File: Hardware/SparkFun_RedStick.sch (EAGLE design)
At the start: 38 parts, among them Q1 DMG2307L, U2 ATMEGA328P_TQFP, U3 CY7C65213, U4 NCP1402, Y1 16MHZ

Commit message: ready for peer review
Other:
- note added: "Boost Regulator"
- note added: "Marshall Taylor"
- note added: "Ports"
- note added: "Power Steering"
- note added: "USB-Serial translation"
- note added: "v01"
- note removed: "3.3v"
- note removed: "5v"
- note removed: "RX (Pin 0)"
- note removed: "TX (Pin 1)"
- note removed: "Voltage Selector"
- moved on the sheet: C10, C11, C3, C4, C5, C6, C7, C8, C9, D1, D2, D3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

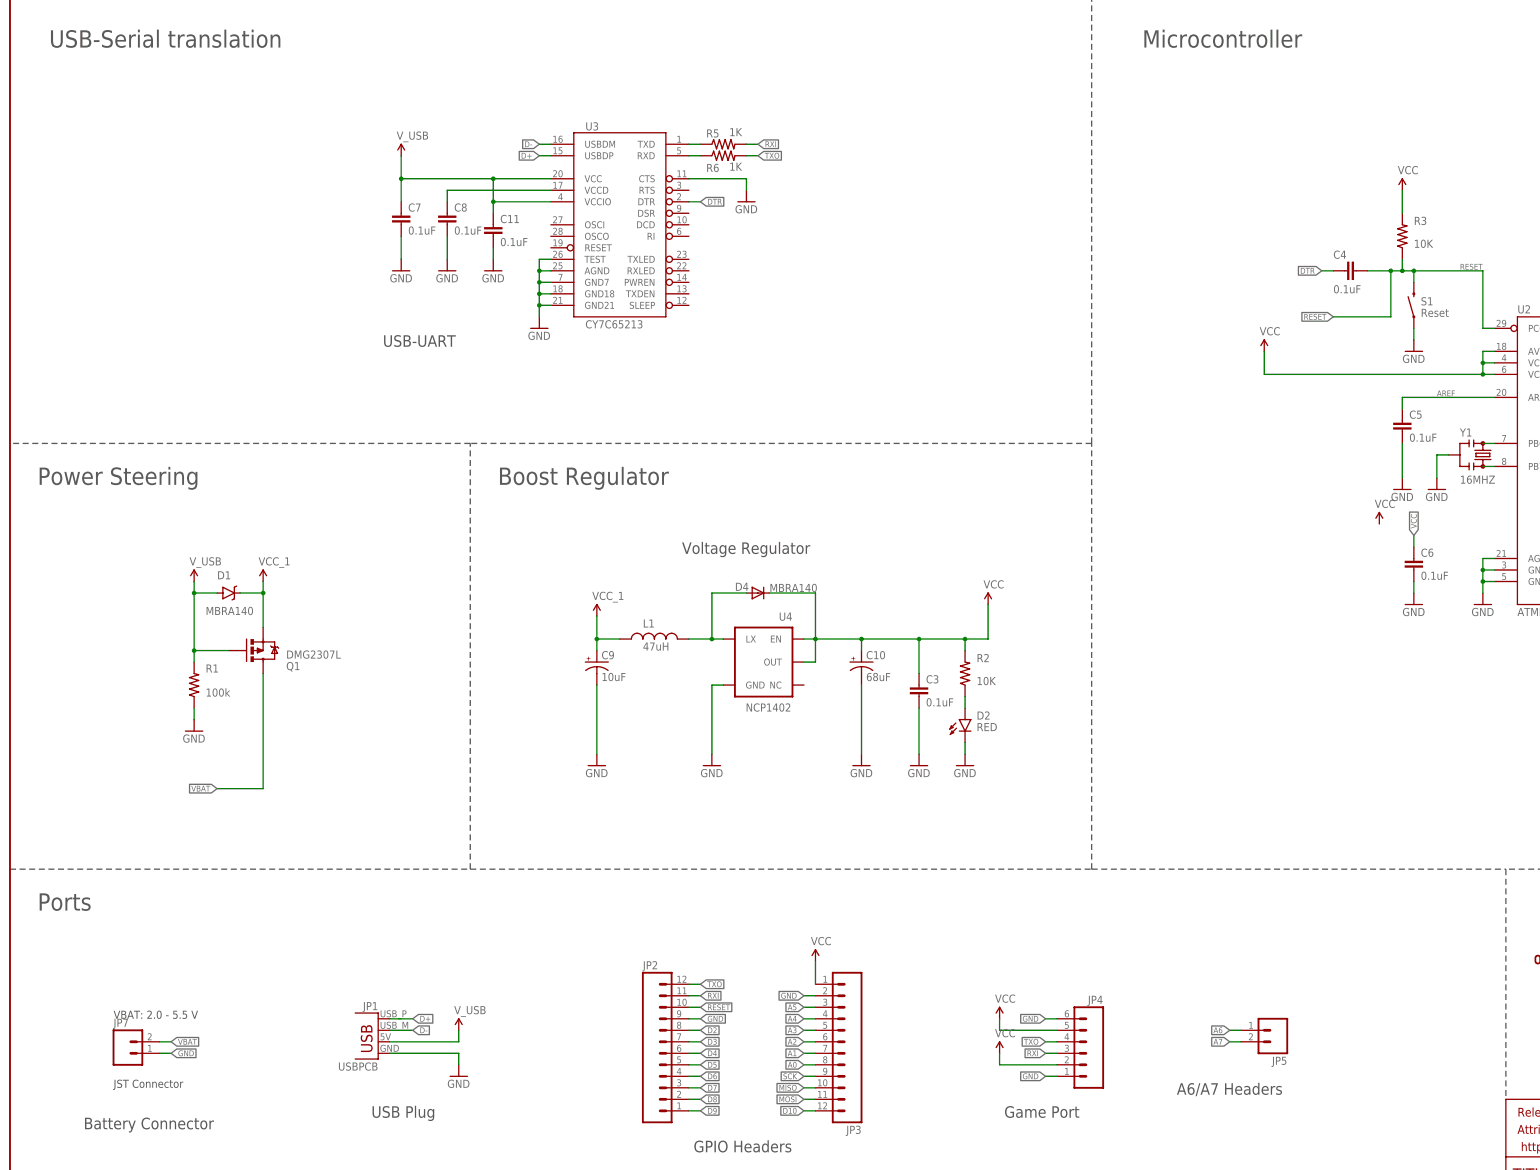
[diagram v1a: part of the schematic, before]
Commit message: New FTDI and serial pinout
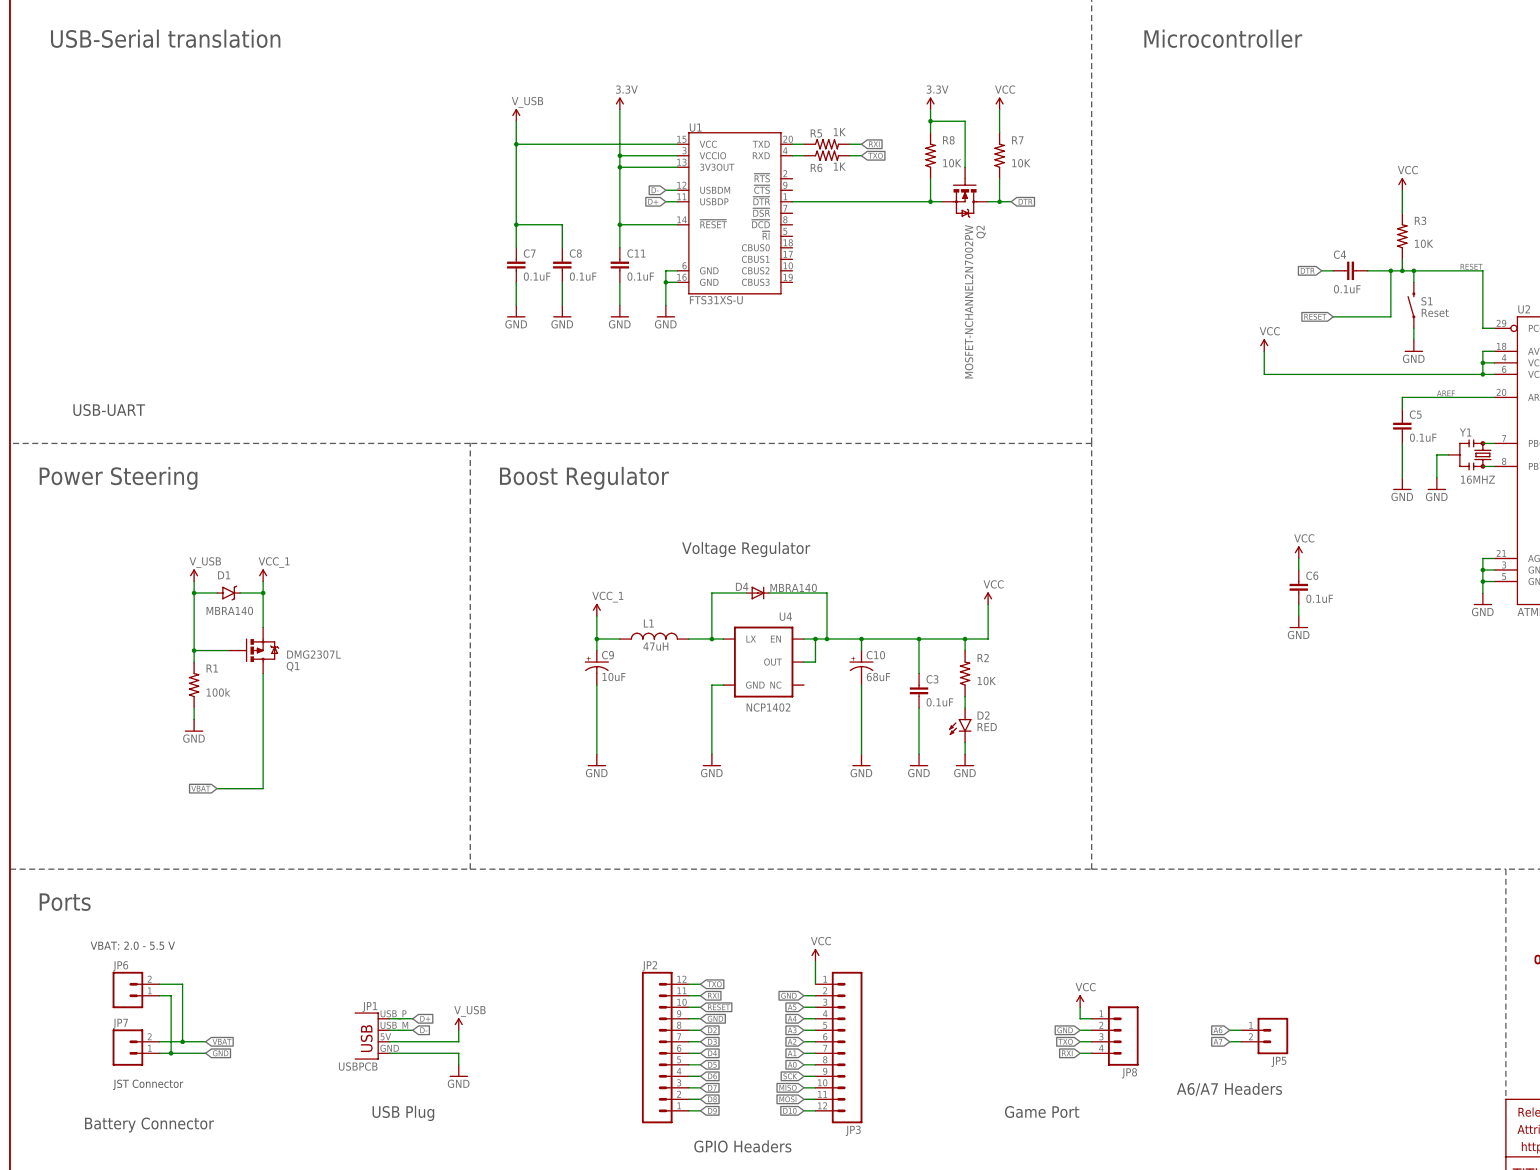
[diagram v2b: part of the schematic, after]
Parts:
- removed JP4: (no value), SparkFun-Connectors:M06NO_SILK_YES_STOP
- removed U3: CY7C65213, SparkFun-DigitalIC:CY7C65213
- added JP6: M021X02_NO_SILK, SparkFun-Connectors:M021X02_NO_SILK
- added JP8: (no value), SparkFun-Connectors:M04PTH
- added Q2: MOSFET-NCHANNEL2N7002PW, SparkFun-DiscreteSemi:MOSFET-NCHANNEL2N7002PW
- added R7, R8: 10K, SparkFun-Resistors:10KOHM-1/10W-1%(0603)0603
- added U1: FTS31XS-U, SparkFun-DigitalIC:FT231XS
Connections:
- removed net N$2: C8.1, U3.VCCD
- new net 3.3V: C11.1, Q2.G, R8.2, U1.!RESET, U1.3V3OUT, U1.VCCIO
- new net N$11: Q2.S, R8.1, U1.!DTR
- net D+: now also U1.USBDP; no longer U3.USBDP
- net D-: now also U1.USBDM; no longer U3.USBDM
- net DTR: now also Q2.D, R7.1; no longer U3.DTR
- net GND: now also JP6.1, JP8.2, U1.GND@16, U1.GND@6; no longer JP4.1, JP4.6, U3.AGND, U3.CTS, U3.GND18, U3.GND21, U3.GND7, U3.TEST
- net N$3: now also U1.TXD; no longer U3.TXD
- net N$7: now also U1.RXD; no longer U3.RXD
- net RXI: now also JP8.4; no longer JP4.3
- net TXO: now also JP8.3; no longer JP4.4
- net VBAT: now also JP6.2
- net VCC: now also JP8.1, R7.2; no longer JP4.2, JP4.5
- net V_USB: now also C8.1, U1.VCC; no longer C11.1, U3.VCC, U3.VCCIO
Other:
- moved on the sheet: C11, C6, C7, C8, R5, R6

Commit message: ready for review
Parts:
- C10: device SparkFun:CAP_POL3528 -> SparkFun-Capacitors:68UF-10V-10%(TANT)
- C9: device SparkFun:CAP_POL1206 -> SparkFun-Capacitors:10UF-16V-10%(TANT)
- D4: device SparkFun:DIODESMA -> SparkFun-DiscreteSemi:DIODE-SCHOTTKY-MBRA140
- JP1: value USBPCB -> USBPCB_NOPASTE; device SparkFun-Connectors:USBPCB -> SparkFun-Connectors:USBPCB_NOPASTE
- JP2, JP3, JP7, JP8: value (none) -> DNP
- L1: device SparkFun:INDUCTORCR54 -> SparkFun-Passives:INDUCTORCR54-47UH
- U4: value NCP1402 -> 5.0v; device SparkFun:V_REG_NCP1400SOT23-5 -> SparkFun-PowerIC:V_REG_NCP1400_5V
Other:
- note added: "2.0-5.0V"
- moved on the sheet: C11, C7, C8, Q2, R5, R6, R7, R8, U1

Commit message: fixed errors
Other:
- note removed: "VBAT: 2.0 - 5.5 V"
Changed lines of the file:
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@@
 <text x="148.336" y="155.956" size="2.54" layer="97">Voltage Regulator</text>
 <text x="16.256" y="28.956" size="2.54" layer="97">Battery Connector</text>
-<text x="17.78" y="68.58" size="1.778" layer="97">VBAT: 2.0 - 5.5 V</text>
 <text x="12.7" y="38.1" size="1.778" layer="97">JST Connector</text>
 <wire x1="101.6" y1="86.36" x2="238.76" y2="86.36" width="0.1524" layer="97" style="longdash"/>

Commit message: Hardware changes for reds review
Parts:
- JP2, JP3: device SparkFun-Connectors:M12LOCK_NO_SILK -> SparkFun-Connectors:M12NO_SILK
- JP8: device SparkFun-Connectors:M04PTH -> SparkFun-Connectors:M04NO_SILK_ALL_ROUND
- R2: value 10K -> 6.8K; device SparkFun-Resistors:10KOHM-1/10W-1%(0603)0603 -> SparkFun-Resistors:6.8KOHM1/10W1%(0603)
- R4: value 330 -> 2.2k; device SparkFun-Resistors:330OHM1/10W1%(0603) -> SparkFun-Resistors:2.2KOHM-1/10W-1%(0603)
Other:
- note added: "2.0-6.0V"
- note added: "v10"
- note removed: "2.0-5.0V"
- note removed: "v01"
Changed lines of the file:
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@@
 <part name="C3" library="SparkFun-Capacitors" deviceset="0.1UF-25V(+80/-20%)(0603)" device="" value="0.1uF"/>
 <part name="D2" library="SparkFun-LED" deviceset="LED-RED" device="0603" value="RED"/>
-<part name="R2" library="SparkFun-Resistors" deviceset="10KOHM-1/10W-1%(0603)" device="0603" value="10K"/>
+<part name="R2" library="SparkFun-Resistors" deviceset="6.8KOHM1/10W1%(0603)" device="" value="6.8K"/>
 <part name="GND6" library="SparkFun-Aesthetics" deviceset="GND" device=""/>
 <part name="GND7" library="SparkFun-Aesthetics" deviceset="GND" device=""/>
@@
 <part name="C6" library="SparkFun-Capacitors" deviceset="0.1UF-25V(+80/-20%)(0603)" device="" value="0.1uF"/>
 <part name="GND11" library="SparkFun-Aesthetics" deviceset="GND" device=""/>
-<part name="R4" library="SparkFun-Resistors" deviceset="330OHM1/10W1%(0603)" device="" value="330"/>
+<part name="R4" library="SparkFun-Resistors" deviceset="2.2KOHM-1/10W-1%(0603)" device="" value="2.2k"/>
 <part name="D3" library="SparkFun-LED" deviceset="LED-GREEN" device="0603" value="GREEN"/>
 <part name="GND12" library="SparkFun-Aesthetics" deviceset="GND" device=""/>
@@
 <part name="R5" library="SparkFun-Resistors" deviceset="1KOHM-1/10W-1%(0603)" device="" value="1K"/>
 <part name="R6" library="SparkFun-Resistors" deviceset="1KOHM-1/10W-1%(0603)" device="" value="1K"/>
-<part name="JP3" library="SparkFun-Connectors" deviceset="M12" device="LOCK_NO_SILK" value="DNP"/>
+<part name="JP3" library="SparkFun-Connectors" deviceset="M12" device="NO_SILK" value="DNP"/>
 <part name="FRAME2" library="SparkFun-Aesthetics" deviceset="FRAME-LEDGER" device=""/>
 <part name="U4" library="SparkFun-PowerIC" deviceset="V_REG_NCP1400" device="_5V" value="5.0v"/>
@@
 <part name="C11" library="SparkFun-Capacitors" deviceset="0.1UF-25V(+80/-20%)(0603)" device="" value="0.1uF"/>
 <part name="GND18" library="SparkFun-Aesthetics" deviceset="GND" device=""/>
-<part name="JP2" library="SparkFun-Connectors" deviceset="M12" device="LOCK_NO_SILK" value="DNP"/>
+<part name="JP2" library="SparkFun-Connectors" deviceset="M12" device="NO_SILK" value="DNP"/>
 <part name="JP7" library="SparkFun-Connectors" deviceset="M02" device="JST-PTH-2" value="DNP"/>
 <part name="GND2" library="SparkFun-Aesthetics" deviceset="GND" device=""/>
@@
 <part name="SUPPLY12" library="SparkFun-Aesthetics" deviceset="VCC" device=""/>
 <part name="JP6" library="SparkFun-Connectors" deviceset="M02" device="1X02_NO_SILK" value="M021X02_NO_SILK"/>
-<part name="JP8" library="SparkFun-Connectors" deviceset="M04" device="PTH" value="DNP"/>
+<part name="JP8" library="SparkFun-Connectors" deviceset="M04" device="NO_SILK_ALL_ROUND" value="DNP"/>
 <part name="GND16" library="SparkFun-Aesthetics" deviceset="GND" device=""/>
 </parts>
@@
 <text x="8.636" y="267.716" size="3.81" layer="97">USB-Serial translation</text>
 <text x="249.936" y="267.716" size="3.81" layer="97">Microcontroller</text>
-<text x="419.862" y="7.112" size="2.54" layer="94">v01</text>
+<text x="419.862" y="7.112" size="2.54" layer="94">v10</text>
 <text x="333.502" y="7.112" size="2.54" layer="94">Marshall Taylor</text>
-<text x="16.256" y="23.876" size="2.54" layer="97">2.0-5.0V</text>
+<text x="16.256" y="23.876" size="2.54" layer="97">2.0-6.0V</text>
 </plain>
 <instances>

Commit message: Getting ready for reds
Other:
- note removed: "USB-UART"
- note removed: "Voltage Regulator"
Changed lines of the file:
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@@
 <?xml version="1.0" encoding="utf-8"?>
 <!DOCTYPE eagle SYSTEM "eagle.dtd">
-<eagle version="7.1.0">
+<eagle version="7.5.0">
 <drawing>
 <settings>
@@
 <layer number="255" name="routoute" color="7" fill="1" visible="no" active="yes"/>
 </layers>
-<schematic xreflabel="%F%N/%S" xrefpart="1_/%S.%C%R">
+<schematic xreflabel="%F%N/%S" xrefpart="/%S.%C%R">
 <attributes>
 </attributes>
@@
 <wire x1="431.8" y1="86.36" x2="330.2" y2="86.36" width="0.1524" layer="97" style="longdash"/>
 <wire x1="0" y1="86.36" x2="101.6" y2="86.36" width="0.1524" layer="97" style="longdash"/>
-<text x="13.716" y="186.436" size="2.54" layer="97">USB-UART</text>
-<text x="148.336" y="155.956" size="2.54" layer="97">Voltage Regulator</text>
 <text x="16.256" y="28.956" size="2.54" layer="97">Battery Connector</text>
 <text x="12.7" y="38.1" size="1.778" layer="97">JST Connector</text>
@@
 </sheet>
 </sheets>
+<errors>
+</errors>
 </schematic>
 </drawing>

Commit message: Re-approved DRC, renamed U4
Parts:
- renumbered U4 to U3
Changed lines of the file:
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@@
 <part name="JP3" library="SparkFun-Connectors" deviceset="M12" device="NO_SILK" value="DNP"/>
 <part name="FRAME2" library="SparkFun-Aesthetics" deviceset="FRAME-LEDGER" device=""/>
-<part name="U4" library="SparkFun-PowerIC" deviceset="V_REG_NCP1400" device="_5V" value="5.0v"/>
+<part name="U3" library="SparkFun-PowerIC" deviceset="V_REG_NCP1400" device="_5V" value="5.0v"/>
 <part name="D4" library="SparkFun-DiscreteSemi" deviceset="DIODE-SCHOTTKY" device="-MBRA140" value="MBRA140"/>
 <part name="C9" library="SparkFun-Capacitors" deviceset="10UF-16V-10%(TANT)" device="" value="10uF"/>
@@
 <instance part="FRAME2" gate="G$1" x="0" y="0"/>
 <instance part="FRAME2" gate="G$2" x="330.2" y="0"/>
-<instance part="U4" gate="G$1" x="167.64" y="132.08" rot="MR0"/>
+<instance part="U3" gate="G$1" x="167.64" y="132.08" rot="MR0"/>
 <instance part="D4" gate="G$1" x="167.64" y="144.78" smashed="yes">
 <attribute name="NAME" x="165.1" y="150.3426" size="1.778" layer="95"/>
@@
 <wire x1="157.48" y1="129.54" x2="154.94" y2="129.54" width="0.1524" layer="91"/>
 <wire x1="154.94" y1="129.54" x2="154.94" y2="111.76" width="0.1524" layer="91"/>
-<pinref part="U4" gate="G$1" pin="GND"/>
+<pinref part="U3" gate="G$1" pin="GND"/>
 <pinref part="GND4" gate="1" pin="GND"/>
 </segment>
@@
 <wire x1="149.86" y1="137.16" x2="154.94" y2="137.16" width="0.1524" layer="91"/>
 <junction x="154.94" y="137.16"/>
-<pinref part="U4" gate="G$1" pin="LX"/>
+<pinref part="U3" gate="G$1" pin="LX"/>
 <pinref part="D4" gate="G$1" pin="A"/>
 <pinref part="L1" gate="G$1" pin="2"/>
@@
 <junction x="177.8" y="134.62"/>
 <junction x="187.96" y="137.16"/>
-<pinref part="U4" gate="G$1" pin="EN"/>
-<pinref part="U4" gate="G$1" pin="OUT"/>
+<pinref part="U3" gate="G$1" pin="EN"/>
+<pinref part="U3" gate="G$1" pin="OUT"/>
 <pinref part="C10" gate="G$1" pin="+"/>
 <pinref part="C3" gate="G$1" pin="1"/>
